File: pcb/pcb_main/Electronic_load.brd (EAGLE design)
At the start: 121.9 x 88.6 mm, 112 parts, among them IC7 LM1117IMPX-5.0, J1 XT60-M, J2 B2B-XH, J3 B4B-XH, J4 B2B-XH, J5 B2B-XH, J6 B2B-XH, J7 B2B-XH, J8 B5B-XH, Q1 IRFP250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

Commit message: poormans rebase xd (im tired...)
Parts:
- R22: value 1k -> 560R
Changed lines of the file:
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@@
 <drawing>
 <settings>
-<setting alwaysvectorfont="yes"/>
+<setting alwaysvectorfont="no"/>
 <setting verticaltext="up"/>
 </settings>
@@
 <attribute name="VALUE" x="77.216" y="33.909" size="1.27" layer="27"/>
 </element>
-<element name="R22" library="rcl" library_urn="urn:adsk.eagle:library:334" package="R0603" package3d_urn="urn:adsk.eagle:package:23555/3" value="1k" x="75.311" y="34.29" smashed="yes" rot="R90">
+<element name="R22" library="rcl" library_urn="urn:adsk.eagle:library:334" package="R0603" package3d_urn="urn:adsk.eagle:package:23555/3" value="560R" x="75.311" y="34.29" smashed="yes" rot="R90">
 <attribute name="NAME" x="75.819" y="30.099" size="1.016" layer="25" rot="R90"/>
 <attribute name="POPULARITY" value="70" x="75.311" y="34.29" size="1.778" layer="27" rot="R90" display="off"/>
@@
 <attribute name="MF" value="Sharp Microelectronics" x="83.82" y="6.985" size="1.778" layer="27" display="off"/>
 <attribute name="MP" value="PC817X2NIP0F" x="83.82" y="6.985" size="1.778" layer="27" display="off"/>
+<attribute name="NAME" x="81.014759375" y="10.0908" size="1.27238125" layer="25"/>
 <attribute name="NAME" x="81.01816875" y="10.08701875" size="1.27083125" layer="25"/>
-<attribute name="NAME" x="81.014759375" y="10.0908" size="1.27238125" layer="25"/>
 <attribute name="PACKAGE" value="SMD-4 Sharp" x="83.82" y="6.985" size="1.778" layer="27" display="off"/>
 <attribute name="PRICE" value="None" x="83.82" y="6.985" size="1.778" layer="27" display="off"/>

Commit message: Add missing component designators on schematic, adjust text size and positioning
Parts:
- U5: value OPA277-SOIC08 -> OPA277
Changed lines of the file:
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@@
 </layers>
 <board>
-<fusionsync huburn="a.YnVzaW5lc3M6Z21haWw1MzQ2MjM" projecturn="a.YnVzaW5lc3M6Z21haWw1MzQ2MjMjRDIwMTkxMjI5MjUwNjU0MjU2" f3durn="urn:adsk.wipprod:dm.lineage:-LBexN8XREiexSCePDhWkA" pcbguid="" lastpulledtime="" lastsyncedchangeguid="" latestrevisionid="7f8de7b2-4f8c-45b9-b999-f944fbece653" lastsyncedrevisionid="7f8de7b2-4f8c-45b9-b999-f944fbece653" lastboardhashguid="efb84410-8e96-f03e-edf5-2a22bf7f7d7c" lastpushedtime="2022-07-31T18:11:28Z" linktopcb3d="true"/>
+<fusionsync huburn="a.YnVzaW5lc3M6Z21haWw1MzQ2MjM" projecturn="a.YnVzaW5lc3M6Z21haWw1MzQ2MjMjRDIwMTkxMjI5MjUwNjU0MjU2" f3durn="urn:adsk.wipprod:dm.lineage:-LBexN8XREiexSCePDhWkA" pcbguid="" lastpulledtime="" lastsyncedchangeguid="" latestrevisionid="7f8de7b2-4f8c-45b9-b999-f944fbece653" lastsyncedrevisionid="7f8de7b2-4f8c-45b9-b999-f944fbece653" lastboardhashguid="efb84410-8e96-f03e-edf5-2a22bf7f7d7c" lastpushedtime="2022-07-31T18:11:28Z" linktopcb3d="false"/>
 <plain>
 <wire x1="0" y1="0" x2="121.9" y2="0" width="0" layer="20"/>
@@
 <attribute name="VALUE" x="86.106" y="30.607" size="1.27" layer="27" rot="R180"/>
 </element>
-<element name="U5" library="OPA277" package="SOIC-08_150MIL" override_package3d_urn="urn:adsk.eagle:package:36503863/2" override_package_urn="urn:adsk.eagle:footprint:36503864/1" value="OPA277-SOIC08" x="75.565" y="21.59" smashed="yes" rot="R90">
+<element name="U5" library="OPA277" package="SOIC-08_150MIL" override_package3d_urn="urn:adsk.eagle:package:36503863/2" override_package_urn="urn:adsk.eagle:footprint:36503864/1" value="OPA277" x="75.565" y="21.59" smashed="yes" rot="R90">
 <attribute name="AVAILABILITY" value="In Stock" x="75.565" y="21.59" size="1.778" layer="27" rot="R90" display="off"/>
 <attribute name="DESCRIPTION" value=" Op Amp Single Low Offset Voltage Amplifier ±18V 8-Pin PDIP Tube " x="75.565" y="21.59" size="1.778" layer="27" rot="R90" display="off"/>
@@
 <attribute name="VALUE" x="58.547" y="22.225" size="1.27" layer="27" rot="R90"/>
 </element>
-<element name="U$3" library="voltage_references" package="SOIC8" package3d_urn="urn:adsk.eagle:package:36503846/2" override_package3d_urn="urn:adsk.eagle:package:36704400/2" override_package_urn="urn:adsk.eagle:footprint:16321/1" value="LM4140" x="95.25" y="35.814" smashed="yes">
+<element name="U$3" library="voltage_references" package="SOIC8" package3d_urn="urn:adsk.eagle:package:36503846/3" override_package3d_urn="urn:adsk.eagle:package:36704400/2" override_package_urn="urn:adsk.eagle:footprint:16321/1" value="LM4140" x="95.25" y="35.814" smashed="yes">
 <attribute name="NAME" x="90.932" y="40.259" size="1.27" layer="25" rot="R270"/>
 <attribute name="VALUE" x="99.187" y="33.909" size="1.27" layer="27" rot="R90"/>

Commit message: Improve schematic, adjust text size and positioning
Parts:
- IC7: value LM1117IMPX-5.0 -> LM1117-5.0
- U$2: value CRYSTAL_3,4X2,7 -> 16MHz
- VR1: value (none) -> TL431
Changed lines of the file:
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@@
 <attribute name="VALUE" x="34.29" y="17.78" size="1.27" layer="27" ratio="10" rot="R180"/>
 </element>
-<element name="VR1" library="tl431" package="TO92-CLP" package3d_urn="urn:adsk.eagle:package:30363/1" override_package3d_urn="urn:adsk.eagle:package:36629198/2" override_package_urn="urn:adsk.eagle:footprint:30307/1" value="" x="29.21" y="19.05" smashed="yes">
+<element name="VR1" library="tl431" package="TO92-CLP" package3d_urn="urn:adsk.eagle:package:30363/1" override_package3d_urn="urn:adsk.eagle:package:36629198/2" override_package_urn="urn:adsk.eagle:footprint:30307/1" value="TL431" x="29.21" y="19.05" smashed="yes">
 <attribute name="NAME" x="32.385" y="19.685" size="1.27" layer="25" ratio="10"/>
 <attribute name="POPULARITY" value="1" x="29.21" y="19.05" size="1.778" layer="27" display="off"/>
@@
 <attribute name="VALUE" x="27.305" y="19.685" size="1.27" layer="27" rot="R90"/>
 </element>
-<element name="IC7" library="lm1117" package="SOT223" override_package3d_urn="urn:adsk.eagle:package:34042167/2" override_package_urn="urn:adsk.eagle:footprint:34042172/1" value="LM1117IMPX-5.0" x="46.99" y="10.16" smashed="yes" rot="R180">
+<element name="IC7" library="lm1117" package="SOT223" override_package3d_urn="urn:adsk.eagle:package:34042167/2" override_package_urn="urn:adsk.eagle:footprint:34042172/1" value="LM1117-5.0" x="46.99" y="10.16" smashed="yes" rot="R180">
 <attribute name="NAME" x="50.8508" y="11.43" size="1.27" layer="25" rot="R270"/>
 <attribute name="VALUE" x="41.8592" y="11.43" size="1.27" layer="27" rot="R270"/>
@@
 <attribute name="MF" value="Sharp Microelectronics" x="83.82" y="6.985" size="1.778" layer="27" display="off"/>
 <attribute name="MP" value="PC817X2NIP0F" x="83.82" y="6.985" size="1.778" layer="27" display="off"/>
+<attribute name="NAME" x="81.01816875" y="10.08701875" size="1.27083125" layer="25"/>
 <attribute name="NAME" x="81.014759375" y="10.0908" size="1.27238125" layer="25"/>
-<attribute name="NAME" x="81.01816875" y="10.08701875" size="1.27083125" layer="25"/>
 <attribute name="PACKAGE" value="SMD-4 Sharp" x="83.82" y="6.985" size="1.778" layer="27" display="off"/>
 <attribute name="PRICE" value="None" x="83.82" y="6.985" size="1.778" layer="27" display="off"/>
@@
 <attribute name="VALUE" x="92.202" y="-0.381" size="1.27" layer="27"/>
 </element>
-<element name="U$2" library="CRYSTAL_SMD_3,4x2.7mm" package="CRYSTAL_3,4X2,7" value="CRYSTAL_3,4X2,7" x="101.6" y="11.43" smashed="yes" rot="MR270"/>
+<element name="U$2" library="CRYSTAL_SMD_3,4x2.7mm" package="CRYSTAL_3,4X2,7" value="16MHz" x="101.6" y="11.43" smashed="yes" rot="MR270"/>
 <element name="C10" library="rcl" library_urn="urn:adsk.eagle:library:334" package="C0603" package3d_urn="urn:adsk.eagle:package:23616/2" value="1u" x="32.385" y="20.32" smashed="yes" rot="MR90">
 <attribute name="NAME" x="33.401" y="19.05" size="1.016" layer="26" rot="MR90"/>

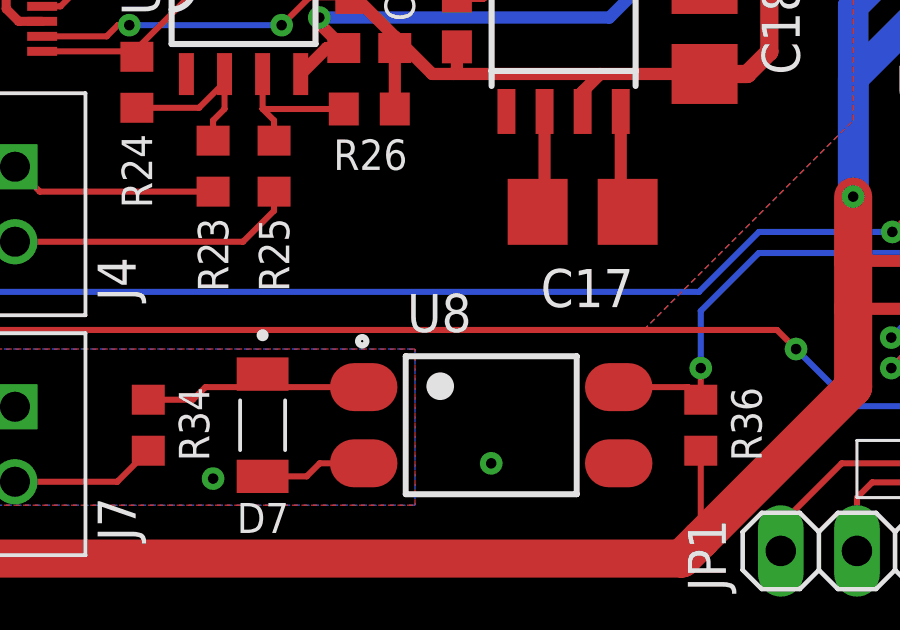
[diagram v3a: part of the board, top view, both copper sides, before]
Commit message: Rename CURRENTx nets to V_SHUNT_x, add negation to OFF net on the main pcb
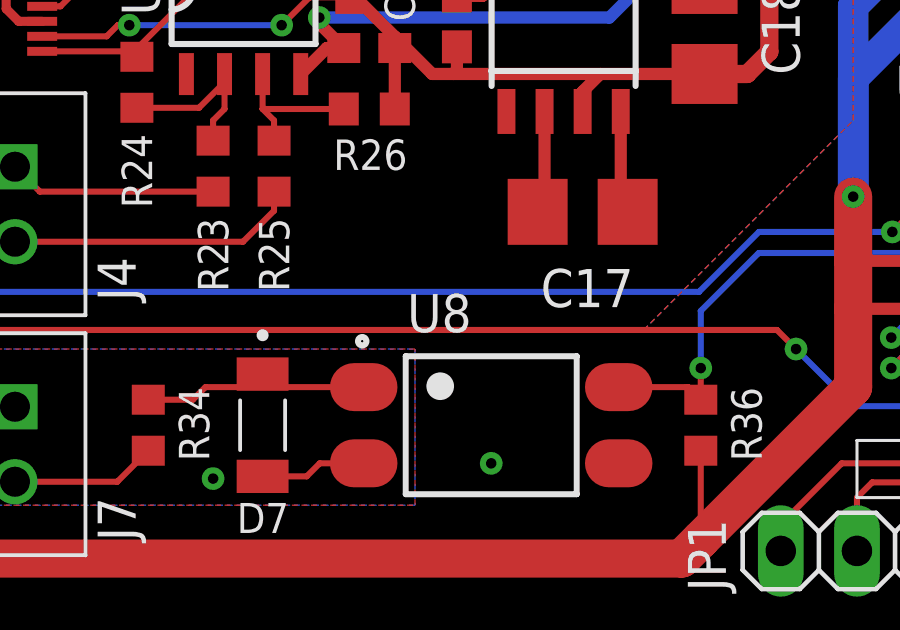
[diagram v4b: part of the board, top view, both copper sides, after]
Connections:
- net CURRENT1 renamed V_SHUNT_1
- net CURRENT2 renamed V_SHUNT_2
- net CURRENT3 renamed V_SHUNT_3
- net CURRENT4 renamed V_SHUNT_4
- net OFF renamed !OFF
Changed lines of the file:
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@@
 <attribute name="MF" value="Sharp Microelectronics" x="83.82" y="6.985" size="1.778" layer="27" display="off"/>
 <attribute name="MP" value="PC817X2NIP0F" x="83.82" y="6.985" size="1.778" layer="27" display="off"/>
+<attribute name="NAME" x="81.014759375" y="10.0908" size="1.27238125" layer="25"/>
 <attribute name="NAME" x="81.01816875" y="10.08701875" size="1.27083125" layer="25"/>
-<attribute name="NAME" x="81.014759375" y="10.0908" size="1.27238125" layer="25"/>
 <attribute name="PACKAGE" value="SMD-4 Sharp" x="83.82" y="6.985" size="1.778" layer="27" display="off"/>
 <attribute name="PRICE" value="None" x="83.82" y="6.985" size="1.778" layer="27" display="off"/>
@@
 <wire x1="67.945" y1="15.601" x2="68.775" y2="14.771" width="0.2032" layer="1"/>
 </signal>
-<signal name="CURRENT1">
+<signal name="V_SHUNT_1">
 <contactref element="Q1" pad="S"/>
 <contactref element="R3" pad="1"/>
@@
 <wire x1="56.642" y1="24.257" x2="56.642" y2="23.71" width="0.4064" layer="1"/>
 </signal>
-<signal name="CURRENT2">
+<signal name="V_SHUNT_2">
 <contactref element="Q2" pad="S"/>
 <contactref element="R8" pad="1"/>
@@
 <wire x1="58.674" y1="24.46889375" x2="58.674" y2="23.71" width="0.4064" layer="1"/>
 </signal>
-<signal name="CURRENT3">
+<signal name="V_SHUNT_3">
 <contactref element="Q3" pad="S"/>
 <contactref element="R13" pad="1"/>
@@
 <wire x1="62.103" y1="25.908" x2="69.088" y2="25.908" width="0.4064" layer="1"/>
 </signal>
-<signal name="CURRENT4">
+<signal name="V_SHUNT_4">
 <contactref element="Q4" pad="S"/>
 <contactref element="R18" pad="1"/>
@@
 <wire x1="56.515" y1="34.925" x2="57.57" y2="34.925" width="0.2032" layer="16"/>
 </signal>
-<signal name="OFF">
+<signal name="!OFF">
 <contactref element="R37" pad="1"/>
 <contactref element="R38" pad="1"/>
